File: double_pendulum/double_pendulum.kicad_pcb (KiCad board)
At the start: 2 copper layers, 106.3 x 128.5 mm, 57 parts, among them J1 Conn_01x21_Socket, J12 Eurorack_Power_16pin_Shrouded, J2 Conn_01x21_Socket, J3 1734839-8, J5 PJ301M-12, J6 PJ301M-12, J7 Conn_02x10_Odd_Even, U1 SC0915, U2 TL072, U3 TL072, U4 MCP4922-E_P, U5 TL072, U6 LM7805_TO220, U7 MCP4922-E_P, U8 TMUX4051PWR, U9 TL072

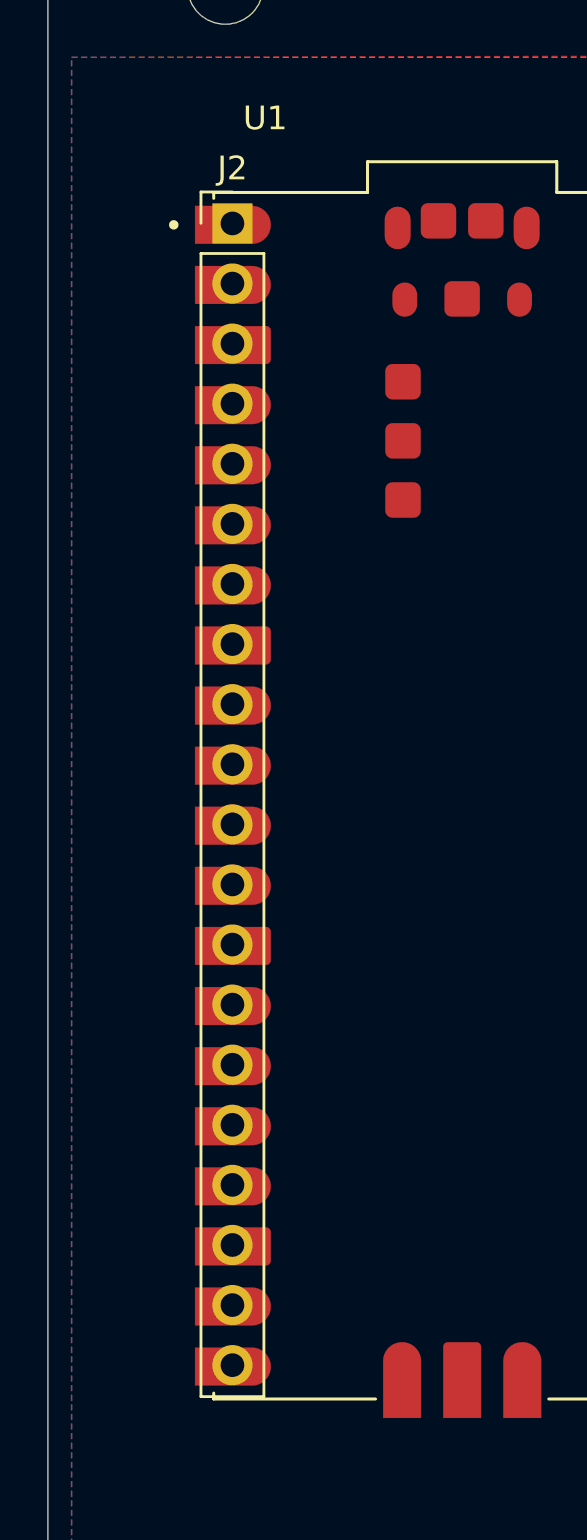
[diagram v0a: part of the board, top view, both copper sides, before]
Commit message: Updated double pendulum with todo notes
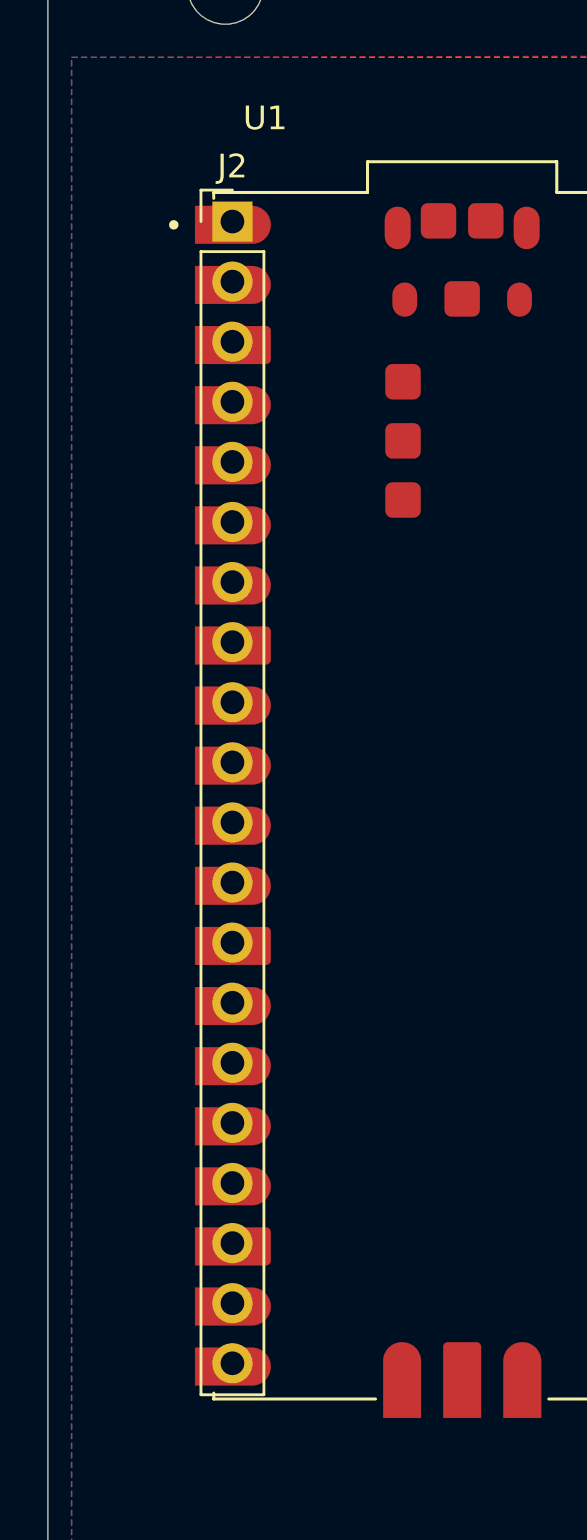
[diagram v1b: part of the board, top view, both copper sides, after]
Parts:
- moved J2 0.08 mm to (44.2, 42.7)
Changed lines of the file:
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@@
 		(at 80.81 58.22)
 		(property "Reference" "U4"
-			(at -3.200445 -19.405915 360)
+			(at -3.200445 -19.405915 0)
 			(layer "F.SilkS")
 			(effects
@@
 		)
 		(property "Value" "MCP4922-E_P"
-			(at 7.85434 4.14321 360)
+			(at 7.85434 4.14321 0)
 			(layer "F.Fab")
 			(effects
@@
 		)
 		(property "Footprint" "MCP4922:DIP254P762X533-14"
-			(at 0 0 360)
+			(at 0 0 0)
 			(layer "F.Fab")
 			(hide yes)
@@
 		)
 		(property "Datasheet" ""
-			(at 0 0 360)
+			(at 0 0 0)
 			(layer "F.Fab")
 			(hide yes)
@@
 		)
 		(property "Description" ""
-			(at 0 0 360)
+			(at 0 0 0)
 			(layer "F.Fab")
 			(hide yes)
@@
 	(footprint "Connector_PinHeader_2.54mm:PinHeader_1x20_P2.54mm_Vertical"
 		(layer "F.Cu")
-		(at 44.2 42.82)
+		(at 44.2 42.74)
 		(descr "Through hole straight pin header, 1x20, 2.54mm pitch, single row")
 		(tags "Through hole pin header THT 1x20 2.54mm single row")
@@
 		)
 		(property "Footprint" "TMUX4051:TSSOP16_PW_TEX"
-			(at 0 0 360)
+			(at 0 0 0)
 			(layer "F.Fab")
 			(hide yes)
@@
 		)
 		(property "Datasheet" "TMUX4051PWR"
-			(at 0 0 360)
+			(at 0 0 0)
 			(layer "F.Fab")
 			(hide yes)
@@
 		)
 		(property "Description" ""
-			(at 0 0 360)
+			(at 0 0 0)
 			(layer "F.Fab")
 			(hide yes)
@@
 		)
 		(fp_text user "*"
-			(at -3.20675 -3.773551 360)
+			(at -3.20675 -3.773551 0)
 			(layer "F.SilkS")
 			(effects
@@
 		)
 		(fp_text user "*"
-			(at -1.8669 -2.4765 360)
+			(at -1.8669 -2.4765 0)
 			(layer "F.Fab")
 			(effects
@@
 		(at 121.6 83.764447 180)
 		(property "Reference" "J3"
-			(at -3.579678 -1.521557 360)
+			(at -3.579678 -1.521557 0)
 			(layer "F.SilkS")
 			(effects
@@
 		)
 		(property "Value" "1734839-8"
-			(at -1.829208 5.474592 360)
+			(at -1.829208 5.474592 0)
 			(layer "F.Fab")
 			(effects
@@
 		)
 		(property "Footprint" "1734839_8:TE_1734839-8"
-			(at 0 0 360)
+			(at 0 0 0)
 			(layer "F.Fab")
 			(hide yes)
@@
 		)
 		(property "Datasheet" ""
-			(at 0 0 360)
+			(at 0 0 0)
 			(layer "F.Fab")
 			(hide yes)
@@
 		)
 		(property "Description" ""
-			(at 0 0 360)
+			(at 0 0 0)
 			(layer "F.Fab")
 			(hide yes)

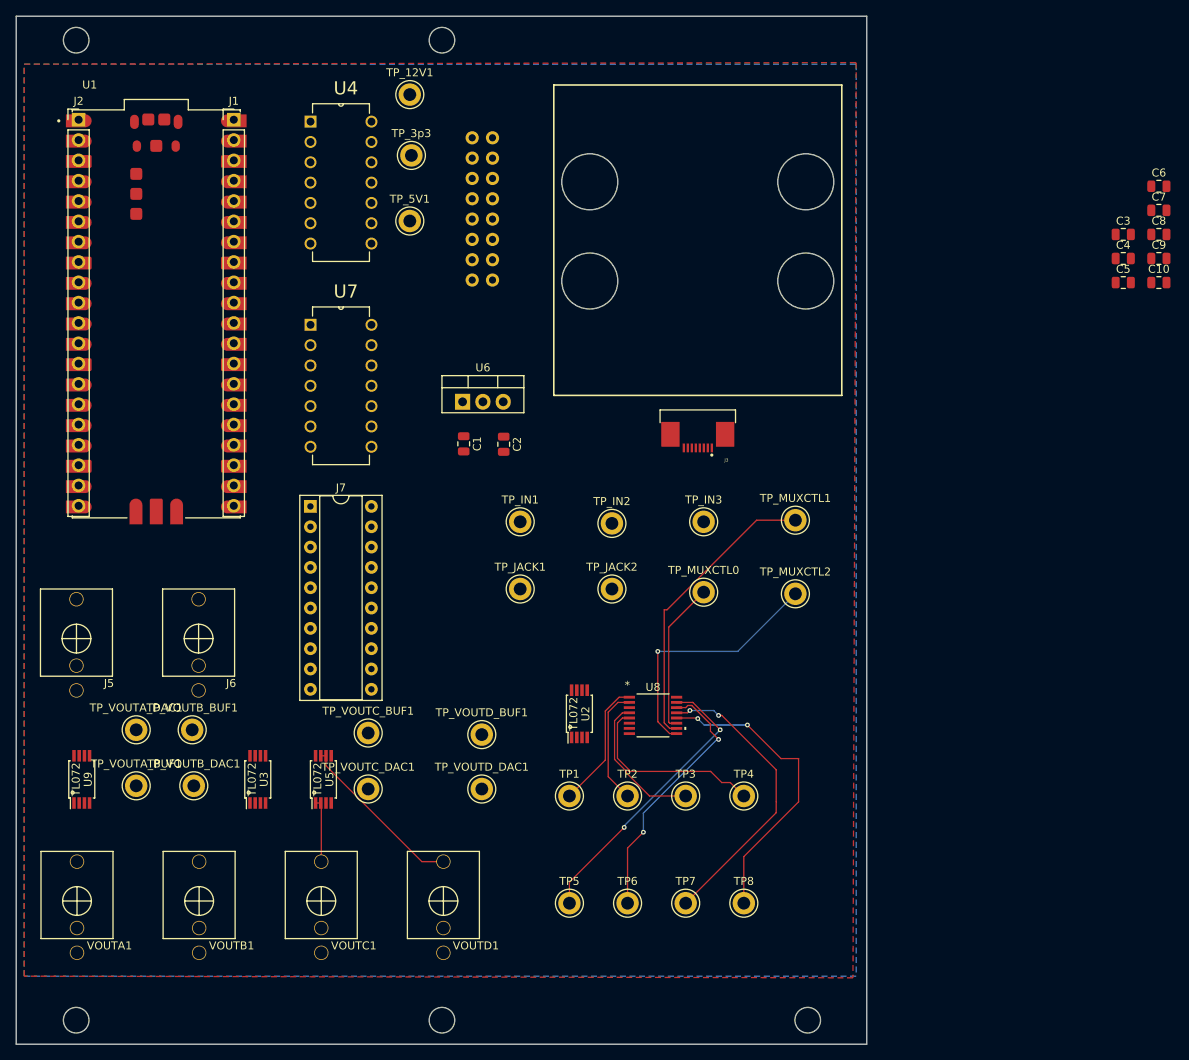
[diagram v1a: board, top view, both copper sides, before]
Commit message: Finished schematic and layout of the double pendulum
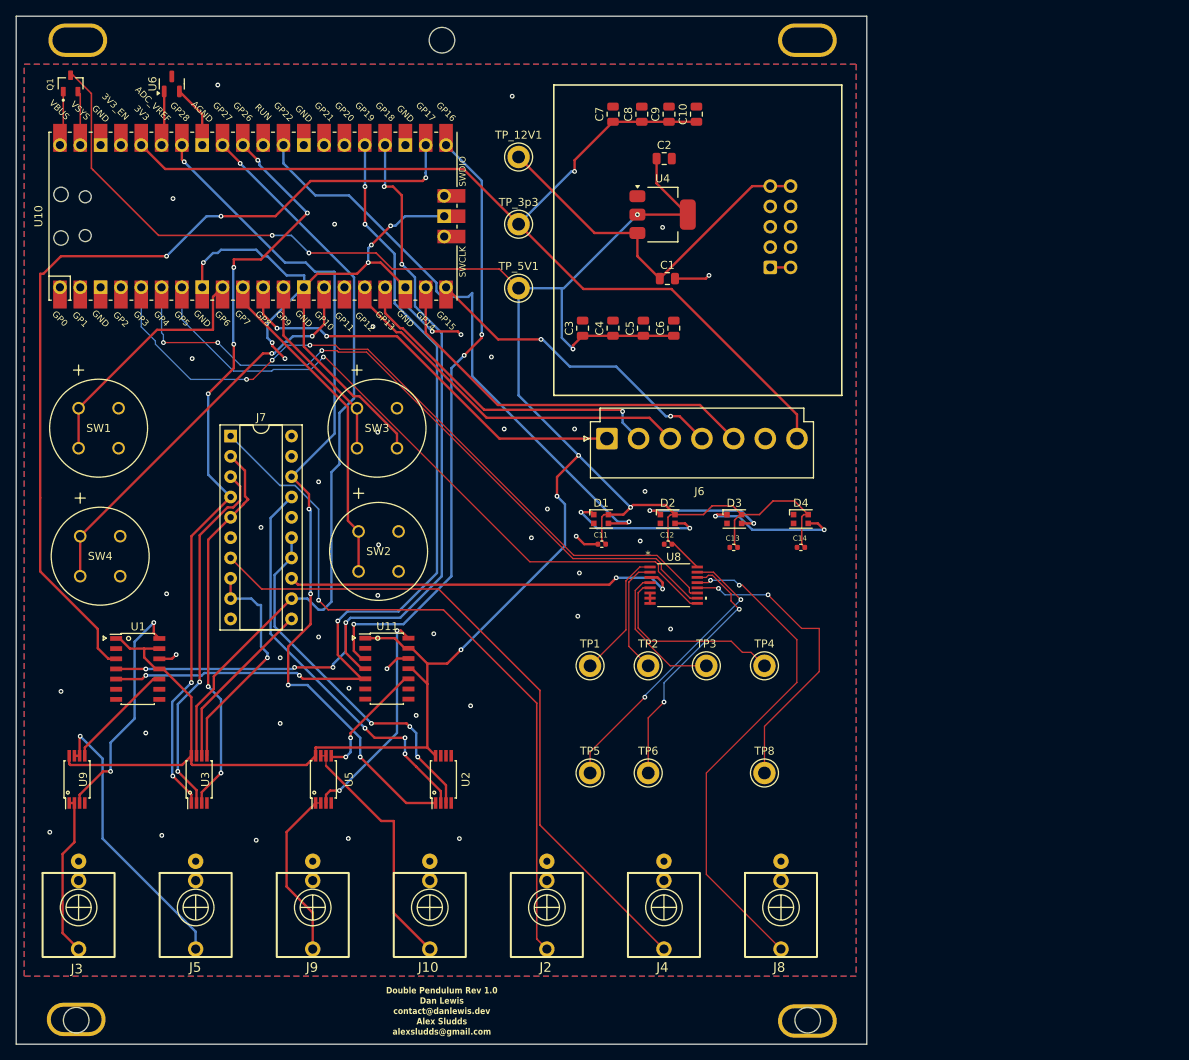
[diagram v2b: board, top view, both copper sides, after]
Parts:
- removed J12: Eurorack_Power_16pin_Shrouded, PCM_4ms_Connector:Pins_2x08_2.54mm_TH_EuroPower_Shrouded
- removed TP7, TP_IN1, TP_IN2, TP_IN3, TP_JACK1, TP_JACK2, TP_MUXCTL0, TP_MUXCTL1, TP_MUXCTL2, TP_VOUTA_BUF1, TP_VOUTA_DAC1, TP_VOUTB_BUF1, TP_VOUTB_DAC1, TP_VOUTC_BUF1, TP_VOUTC_DAC1, TP_VOUTD_BUF1, TP_VOUTD_DAC1: TestPoint, TestPoint:TestPoint_Keystone_5005-5009_Compact
- removed U7: MCP4922-E_P, MCP4922:DIP254P762X533-14
- removed VOUTA1, VOUTB1, VOUTC1, VOUTD1: PJ301M-12, Eurocad:PJ301M-12
- added C11: 100nF_0402_16V, 4ms_Capacitor:C_0402, F.Cu at (109.6, 95.8)
- added C12: 100nF_0402_16V, 4ms_Capacitor:C_0402, F.Cu at (117.9, 95.8)
- added C13: 100nF_0402_16V, 4ms_Capacitor:C_0402, F.Cu at (126.1, 96.2)
- added C14: 100nF_0402_16V, 4ms_Capacitor:C_0402, F.Cu at (134.5, 96.2)
- added D1: WS2812B-2020, LED_SMD:LED_WS2812B-2020_PLCC4_2.0x2.0mm, F.Cu at (109.5, 92.7)
- added D2: WS2812B-2020, LED_SMD:LED_WS2812B-2020_PLCC4_2.0x2.0mm, F.Cu at (117.8, 92.7)
- added D3: WS2812B-2020, LED_SMD:LED_WS2812B-2020_PLCC4_2.0x2.0mm, F.Cu at (126.2, 92.7)
- added D4: WS2812B-2020, LED_SMD:LED_WS2812B-2020_PLCC4_2.0x2.0mm, F.Cu at (134.5, 92.7)
- added H1: MountingHole, 4ms_Faceplate:Faceplate_Rail_Mount_Slot_Plated, F.Cu at (135.3, 155.4)
- added H2: MountingHole, 4ms_Faceplate:Faceplate_Rail_Mount_Slot_Plated, F.Cu at (43.9, 155.2)
- added H3: MountingHole, 4ms_Faceplate:Faceplate_Rail_Mount_Slot_Plated, F.Cu at (44.1, 26.8)
- added H4: MountingHole, 4ms_Faceplate:Faceplate_Rail_Mount_Slot_Plated, F.Cu at (135.3, 32.8)
- added J10: 3.5mm_Mono_Switched_sm, 4ms_Jack:EighthInch_PJ398SM, F.Cu at (88.1, 141.2)
- added J4: 3.5mm_Mono_Switched_sm, 4ms_Jack:EighthInch_PJ398SM, F.Cu at (117.4, 141.2)
- added J8: 3.5mm_Mono_Switched_sm, 4ms_Jack:EighthInch_PJ398SM, F.Cu at (132.0, 141.2)
- added J9: 3.5mm_Mono_Switched_sm, 4ms_Jack:EighthInch_PJ398SM, F.Cu at (73.5, 141.2)
- added Q1: DMG2305UX-7, DMG2305UX_7:SOT91P240X110-3N_DMG2305UX-7, F.Cu at (43.2, 38.2)
- added SW1: D6R90F2LFS, D6R90:D6R90_CNK, F.Cu at (44.2, 78.8)
- added SW2: D6R90F2LFS, D6R90:D6R90_CNK, F.Cu at (79.2, 94.2)
- added SW3: D6R90F2LFS, D6R90:D6R90_CNK, F.Cu at (79.0, 78.8)
- added SW4: D6R90F2LFS, D6R90:D6R90_CNK, F.Cu at (44.4, 94.8)
- added U10: Pico, MCU_RaspberryPi_and_Boards:RPi_Pico_SMD_TH, F.Cu at (66.0, 54.8)
- added U11: MCP4922-ESL, 4ms_Package_SOIC:SOIC-14_3.9x8.65mm_Pitch1.27mm, F.Cu at (82.7, 111.4)
- C1: value 0.33u -> 0.1uF_0805_50V
- C2: value 0.33u -> 10uF_0603_10V
- J1: value Conn_01x21_Socket -> Eurorack_Power_10pin_Shrouded; footprint Connector_PinHeader_2.54mm:PinHeader_1x20_P2.54mm_Vertical -> 4ms_Connector:Pins_2x05_2.54mm_TH_EurorackPower_Shrouded; moved to B.Cu
- J2: value Conn_01x21_Socket -> 3.5mm_Mono_Switched_sm; footprint Connector_PinHeader_2.54mm:PinHeader_1x20_P2.54mm_Vertical -> 4ms_Jack:EighthInch_PJ398SM
- J3: value 1734839-8 -> 3.5mm_Mono_Switched_sm; footprint 1734839_8:TE_1734839-8 -> 4ms_Jack:EighthInch_PJ398SM
- J5: value PJ301M-12 -> 3.5mm_Mono_Switched_sm; footprint Eurocad:PJ301M-12 -> 4ms_Jack:EighthInch_PJ398SM
- J6: value PJ301M-12 -> Conn_01x07; footprint Eurocad:PJ301M-12 -> Connector_JST:JST_VH_B7P-VH_1x07_P3.96mm_Vertical
- U1: value SC0915 -> MCP4922-ESL; footprint SC0915:MODULE_SC0915 -> 4ms_Package_SOIC:SOIC-14_3.9x8.65mm_Pitch1.27mm
- U2, U3, U5, U9: footprint PCM_4ms_Package_SSOP:TSSOP-8_4.4x3mm_Pitch0.65mm -> 4ms_Package_SSOP:TSSOP-8_4.4x3mm_Pitch0.65mm
- U4: value MCP4922-E_P -> LD1117S50TR_SOT223; footprint MCP4922:DIP254P762X533-14 -> Package_TO_SOT_SMD:SOT-223-3_TabPin2
- U6: value LM7805_TO220 -> LM4040DBZ-3; footprint Package_TO_SOT_THT:TO-220-3_Vertical -> Package_TO_SOT_SMD:SOT-23
- moved J2 114.5 mm to (102.7, 141.2), turned to 90 degrees
- moved J3 96.4 mm to (44.2, 141.2), turned to 90 degrees
- moved J1 69.6 mm to (131.9, 56.1), turned to 180 degrees
- moved C7 69.3 mm to (111.0, 42.0), turned to 90 degrees
- moved C3 68.6 mm to (107.2, 68.8), turned to 90 degrees
- moved C8 66.4 mm to (114.6, 42.0), turned to 90 degrees
- moved C4 64.4 mm to (111.0, 68.8), turned to 90 degrees
- moved C9 63.8 mm to (118.0, 42.0), turned to 90 degrees
- moved C6 63.2 mm to (118.6, 68.8), turned to 90 degrees
- moved C10 61.5 mm to (121.4, 42.0), turned to 90 degrees
- moved C5 60.3 mm to (114.8, 68.8), turned to 90 degrees
- moved J6 56.8 mm to (110.2, 82.6)
- moved U6 53.9 mm to (55.9, 38.3), turned to 90 degrees
- moved U1 44.5 mm to (51.6, 111.4)
- moved C2 41.0 mm to (117.4, 47.6), turned to 0 degrees
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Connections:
- C1 pad 1: 12V -> +12V
- C1 pad 2: RES3B -> GND
- C10 pad 2: RES3B -> GND
- C2 pad 2: RES3B -> GND
- C3 pad 2: RES3B -> GND
- C4 pad 2: RES3B -> GND
- C5 pad 2: RES3B -> GND
- C6 pad 2: RES3B -> GND
- C7 pad 2: RES3B -> GND
- C8 pad 2: RES3B -> GND
- C9 pad 2: RES3B -> GND
- J1 pad 1: unconnected-(J1-Pin_1-Pad1) -> -12VA
- J1 pad 10: unconnected-(J1-Pin_10-Pad10) -> +12V
- J1 pad 2: unconnected-(J1-Pin_2-Pad2) -> -12VA
- J1 pad 3: unconnected-(J1-Pin_3-Pad3) -> GND
- J1 pad 4: unconnected-(J1-Pin_4-Pad4) -> GND
- J1 pad 5: unconnected-(J1-Pin_5-Pad5) -> GND
- J1 pad 6: unconnected-(J1-Pin_6-Pad6) -> GND
- J1 pad 7: unconnected-(J1-Pin_7-Pad7) -> GND
- J1 pad 8: unconnected-(J1-Pin_8-Pad8) -> GND
- J1 pad 9: unconnected-(J1-Pin_9-Pad9) -> +12V
- J2 pad 1: unconnected-(J2-Pin_1-Pad1) -> RES1A
- J2 pad 2: unconnected-(J2-Pin_2-Pad2) -> GND
- J2 pad 3: unconnected-(J2-Pin_3-Pad3) -> GND
- J3 pad 1: BLK_DISPLAY -> Net-(J3-SIG)
- J3 pad 2: CS_DISPLAY -> GND
- J3 pad 3: DC_DISPLAY -> GND
- J5 pad 1: RES3B -> Net-(J5-SIG)
- J5 pad 2: RES3B -> GND
- J5 pad 3: RES1A -> GND
- J6 pad 1: RES3B -> RES_DISPLAY
- J6 pad 2: RES3B -> CS_DISPLAY
- J6 pad 3: RES4A -> DC_DISPLAY
- J7 pad 10: RES3B -> GND
- J7 pad 16: RES3B -> GND
- J7 pad 6: RES3B -> GND
- TP_12V1 pad 1: 12V -> +12V
- U1 pad 1: unconnected-(U1-GP0-Pad1) -> 5V
- U1 pad 10: unconnected-(U1-GP7-Pad10) -> VOUTB
- U1 pad 11: RES_DISPLAY -> 5V
- U1 pad 12: unconnected-(U1-GP9-Pad12) -> GND
- U1 pad 13: RES3B -> 5V
- U1 pad 14: unconnected-(U1-GP10-Pad14) -> VOUTA
- U1 pad 3: RES3B -> CS_DAC1
- U1 pad 4: unconnected-(U1-GP2-Pad4) -> SCK_DAC
- U1 pad 5: MUXCTL0 -> SDI_DAC
- U1 pad 6: MUXCTL1 -> unconnected-(U1-NC-Pad6)
- U1 pad 7: MUXCTL2 -> unconnected-(U1-NC-Pad7)
- U1 pad 8: RES3B -> unconnected-(U1-~{LDAC}-Pad8)
- U2 pad 4: RES3B -> GND
- U2 pad 8: 3v3 -> 5V
- U3 pad 4: RES3B -> GND
- U3 pad 8: 3v3 -> 5V
- U4 pad 1: 5V -> GND
- U4 pad 2: unconnected-(U4-NC_2-Pad2) -> 5V
- U4 pad 3: CS_DAC1 -> +12V
- U5 pad 4: RES3B -> GND
- U6 pad 1: 12V -> ADC_VREF
- U6 pad 2: RES3B -> GND
- U6 pad 3: 5V -> unconnected-(U6-NC-Pad3)
- U8 pad 6: RES3B -> GND
- U8 pad 7: RES3B -> GND
- U8 pad 8: RES3B -> GND
- U9 pad 1: Net-(U9A--) -> Net-(J3-SIG)
- U9 pad 2: Net-(U9A--) -> Net-(J3-SIG)
- U9 pad 4: (no net) -> GND
- U9 pad 6: Net-(U9B--) -> Net-(J5-SIG)
- U9 pad 7: Net-(U9B--) -> Net-(J5-SIG)
- U9 pad 8: (no net) -> 5V
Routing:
- net 5V: track 0.00 -> 343.9 mm, vias 0 -> 8
- net 3v3: track 0.00 -> 127.3 mm, vias 0 -> 1
- net GND: track 0.00 -> 117.5 mm, vias 0 -> 49
- net SDI_DAC: track 0.00 -> 112.8 mm, vias 0 -> 5
- net SCK_DAC: track 0.00 -> 112.5 mm, vias 0 -> 6
- net CS_DAC1: track 0.00 -> 109.9 mm, vias 0 -> 3
- net IN3: track 0.00 -> 108.6 mm, vias 0 -> 5
- net IN1: track 0.00 -> 97.9 mm, vias 0 -> 7
- net IN2: track 0.00 -> 95.6 mm, vias 0 -> 1
- net RES1A: track 0.00 -> 90.0 mm, vias 0 -> 1
- net RES4A: track 0.00 -> 84.3 mm
- net CS_DAC2: track 0.00 -> 77.2 mm, vias 0 -> 3
- net Net-(D1-DIN): track 0.00 -> 73.8 mm, vias 0 -> 1
- net MUXCTL0: track 19.1 -> 92.3 mm, vias 0 -> 3
- net MUXCTL2: track 31.9 -> 85.1 mm
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- added copper zone on B.Cu, net GND
- added copper zone on F.Cu, net GND
- removed copper zone on B.Cu, net (none)
- removed copper zone on F.Cu, net (none)
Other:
- outline, holes or cut-outs redrawn
- board text added: "Double Pendulum Rev 1.0 Dan Lewis contact@danlewis.dev Alex Sludds alexsludds@gmail.com"
